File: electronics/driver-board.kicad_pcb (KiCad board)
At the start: 2 copper layers, 40 x 40 mm, 62 parts, among them J1 Conn_01x02, J3 Motor_Conn_01x04, J5 Conn_01x06_Female, SW1 SW_Push, SW2 SW_Push, U2 LMR16020PDDAR, U3 ESP32-C6-MINI-1/U, U4 AMS1117-3.3, U5 TMC5240-TSSOP38, U7 AS5047D

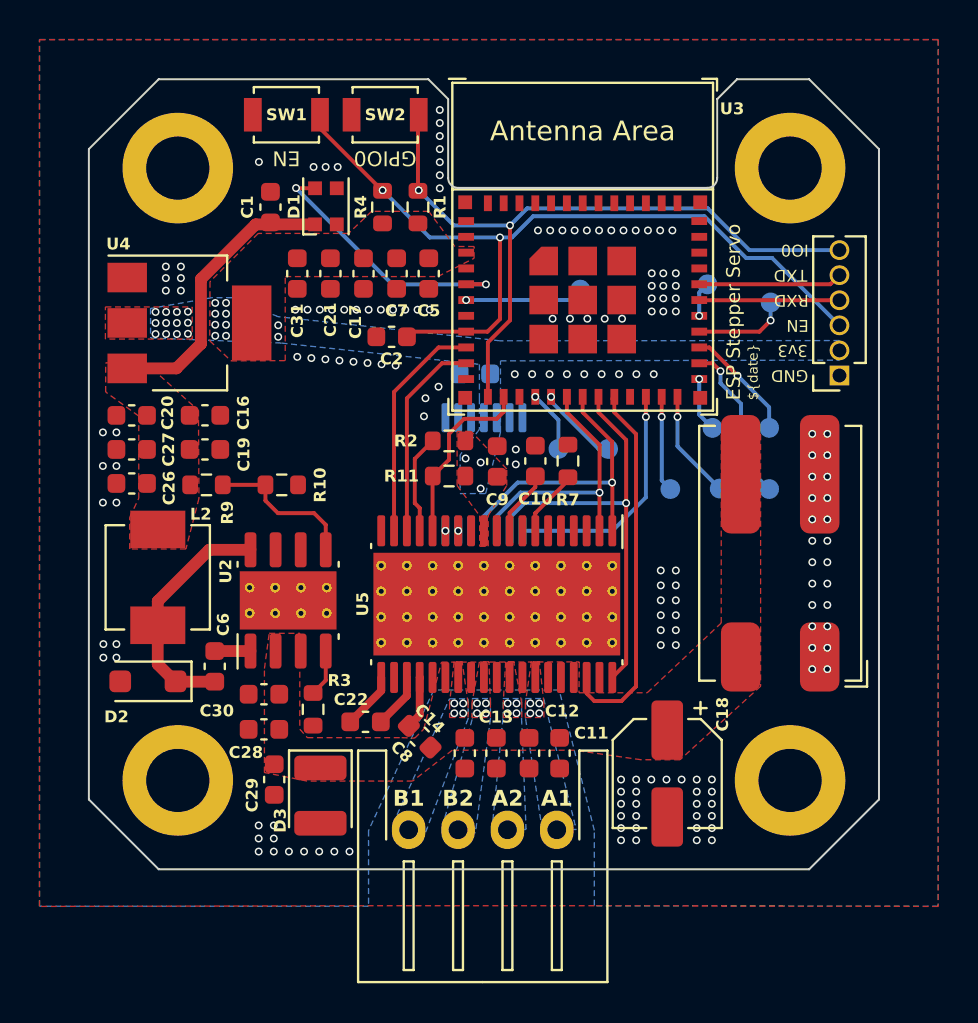
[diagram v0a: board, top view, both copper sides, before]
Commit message: splitted power cap into two and changed connector to wago
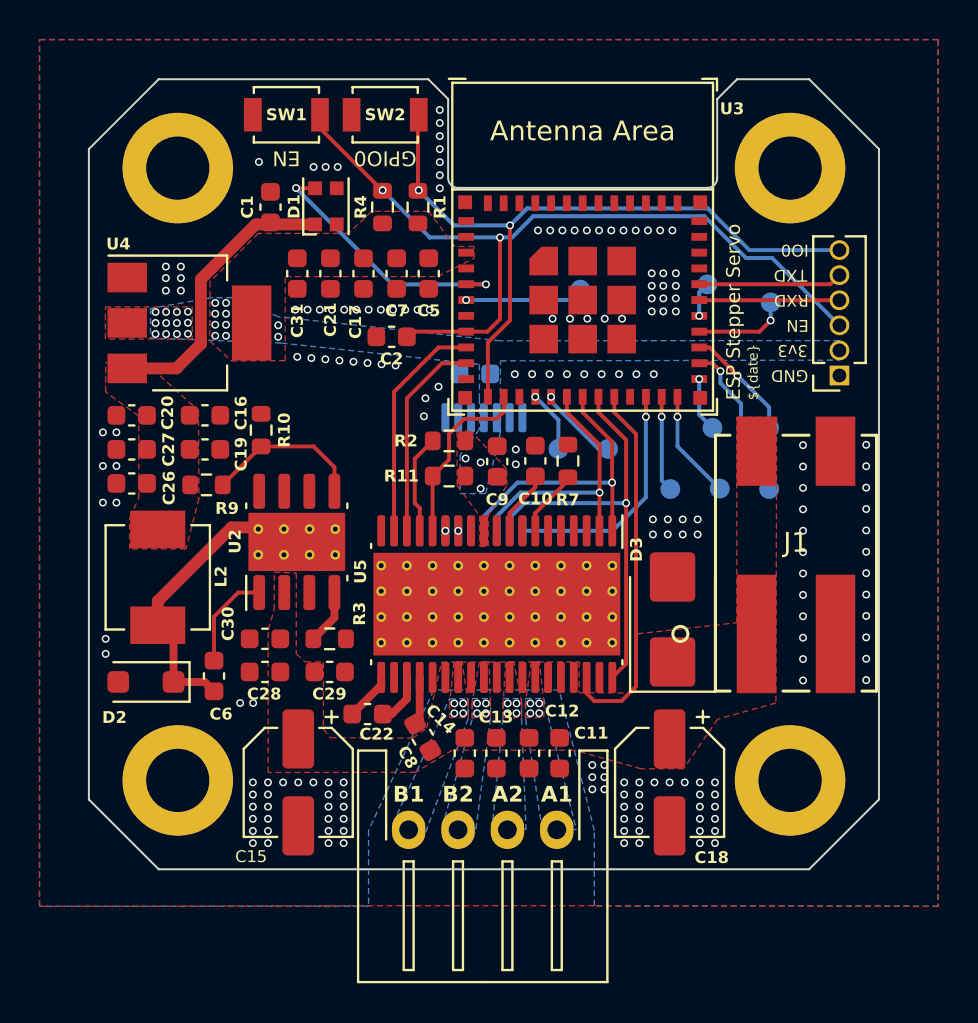
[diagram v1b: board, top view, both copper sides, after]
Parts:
- added C15: 27µF, Capacitor_SMD:CP_Elec_5x5.9, F.Cu at (40.6, 65.6)
- C18: value 47µF -> 27µF
- D3: footprint Diode_SMD:D_1210_3225Metric -> Diode_SMD:D_SMB
- J1: footprint Connector_TE-Connectivity:TE_2834006-2_1x02_P4.0mm_Horizontal -> Slimc_Connector_Wago:2060-472&slash_998-404
- moved D3 19.9 mm to (59.6, 57.3), turned to 90 degrees
- moved C29 6.13 mm to (42.2, 60.0), turned to 180 degrees
- moved R3 3.67 mm to (42.2, 58.3), turned to 180 degrees
- moved U2 2.99 mm to (40.5, 53.4)
- moved R10 2.96 mm to (38.7, 47.8), turned to -90 degrees
- moved C28 2.91 mm to (38.9, 60.0)
- moved C30 2.81 mm to (38.9, 58.3)
- moved J1 0.94 mm to (65.8, 54.5), turned to 0 degrees
- moved C6 0.49 mm to (36.3, 60.2)
- moved C18 0.46 mm to (59.4, 65.6)
- moved C22 0.41 mm to (44.1, 62.1)
- moved C8 0.15 mm to (46.9, 63.3), turned to -60 degrees
- moved D2 0.10 mm to (32.9, 60.5)
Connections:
- J1 pad 1: GND -> VBUS
- J1 pad 2: VBUS -> GND
- U5 pad 39: (no net) -> GND
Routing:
- net Net-(U2-BOOT): track 1.81 -> 5.02 mm
- net Net-(U2-FB): track 7.78 -> 9.38 mm
- net Net-(D2-K): track 12.2 -> 13.1 mm
- net GND: vias 164 -> 182

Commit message: fixed tmc5240 fp and esp32 boot pins
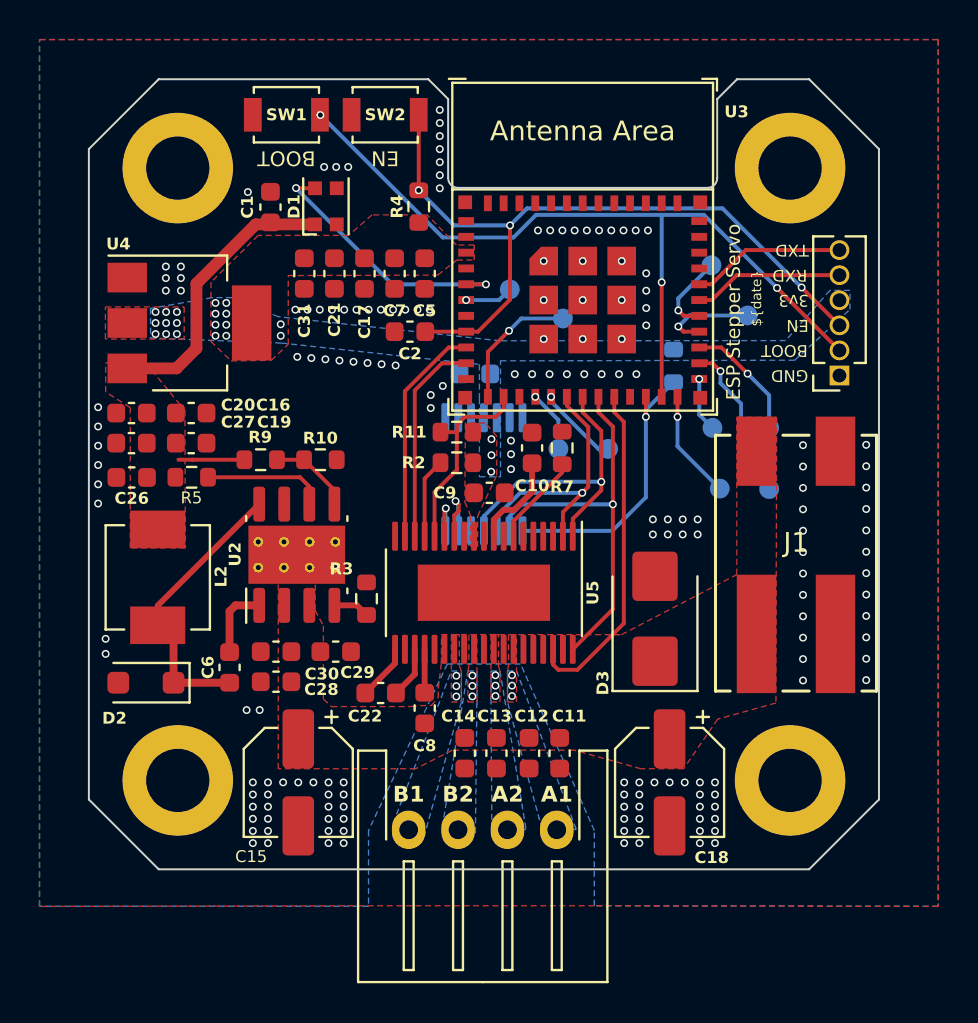
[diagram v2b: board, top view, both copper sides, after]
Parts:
- added R5: 100K, Resistor_SMD:R_0603_1608Metric, F.Cu at (35.2, 50.2)
- R1: moved to B.Cu
- U5: footprint Package_SO:HTSSOP-38-1EP_6.1x12.5mm_P0.65mm_EP5.2x12.5mm_Mask3.39x6.35mm_ThermalVias -> Slimc_Package_SO:TSSOP-38_4.4x9.7mm_P0.5mm
- moved R1 15.2 mm to (59.6, 44.5), turned to -90 degrees
- moved TP9 10.2 mm to (54.0, 42.1)
- moved TP6 3.57 mm to (51.3, 40.6)
- moved R10 3.35 mm to (41.7, 49.3), turned to 180 degrees
- moved R9 3.02 mm to (38.7, 49.3)
- moved R3 2.76 mm to (44.1, 56.3), turned to -90 degrees
- moved R11 2.26 mm to (48.6, 47.9)
- moved R4 1.83 mm to (46.7, 36.4)
- moved C9 1.64 mm to (50.3, 50.9), turned to 180 degrees
- moved C8 1.48 mm to (47.0, 61.8), turned to -90 degrees
- moved TP4 1.34 mm to (63.3, 42.0)
- moved C22 1.26 mm to (44.8, 61.1)
- moved R2 1.17 mm to (48.6, 49.4)
- moved C29 1.07 mm to (42.5, 59.0)
- moved TP5 0.99 mm to (61.5, 39.4)
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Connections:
- J5 pad 2: +3V3 -> /ESP_BOOT
- J5 pad 4: /ESP_UART_RXD -> +3V3
- J5 pad 5: /ESP_UART_TXD -> /ESP_UART_RXD
- J5 pad 6: /ESP_IO0 -> /ESP_UART_TXD
- R1 pad 2: /ESP_IO0 -> /SPI_CSN_ENC
- SW1 pad 2: /ESP_EN -> /ESP_BOOT
- SW2 pad 2: /ESP_IO0 -> /ESP_EN
- TP9 pad 1: Net-(U3-GPIO9) -> Net-(U3-GPIO0/ADC1_CH0/XTAL_32K_P)
- U2 pad 3: unconnected-(U2-EN-Pad3) -> VBUS
- U2 pad 6: unconnected-(U2-PGOOD-Pad6) -> Net-(U2-PGOOD)
- U3 pad 12: /ESP_IO0 -> Net-(U3-GPIO0/ADC1_CH0/XTAL_32K_P)
- U3 pad 23: Net-(U3-GPIO9) -> /ESP_BOOT
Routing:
- net /ESP_BOOT: track 0.00 -> 42.1 mm, vias 0 -> 3
- net /ESP_IO0: track 36.3 -> 0.00 mm, vias 2 -> 0
- net Net-(U3-GPIO0/ADC1_CH0/XTAL_32K_P): track 0.00 -> 6.78 mm, vias 0 -> 1
- net Net-(U2-PGOOD): track 0.00 -> 6.39 mm
- net Net-(U2-FB): track 9.38 -> 4.26 mm
- net Net-(U3-GPIO9): track 4.85 -> 0.00 mm, vias 1 -> 0
- net /ESP_EN: track 41.3 -> 37.5 mm, vias 2 -> 3
- net Net-(U3-GPIO3/ADC1_CH3): track 6.00 -> 2.46 mm
- net Net-(U5-ENCB): track 0.00 -> 3.49 mm
- net +5V: track 14.4 -> 17.8 mm
- net Net-(U5-ENCA): track 0.00 -> 2.58 mm
- net Net-(U3-GPIO23): track 1.77 -> 4.15 mm
- net /SPI_CSN_ENC: track 12.0 -> 14.4 mm
- net /SPI_SCK: track 22.0 -> 20.2 mm
- net /SPI_CSN_TMC: track 19.0 -> 17.2 mm
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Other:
- board text added: "BOOT"
- board text removed: "GPIO0"
- board text removed: "IO9"

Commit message: power labels
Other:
- board text added: "+"
- board text added: "-"
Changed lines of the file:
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@@
     (effects (font (size 0.6 0.6) (thickness 0.1)) (justify left))
+  )
+  (gr_text "+" (at 63.799999 61.8744) (layer "F.SilkS")
+    (effects (font (size 1.5 1.5) (thickness 0.3) bold))
   )
   (gr_text "A2" (at 51.19 66.2052) (layer "F.SilkS" knockout)
@@
     (effects (font (size 0.6 0.6) (thickness 0.1)) (justify left))
   )
+  (gr_text "-" (at 67.800001 61.8744) (layer "F.SilkS")
+    (effects (font (size 1.5 1.5) (thickness 0.3) bold))
+  )
   (gr_text "B1" (at 46.19 66.2052) (layer "F.SilkS" knockout)

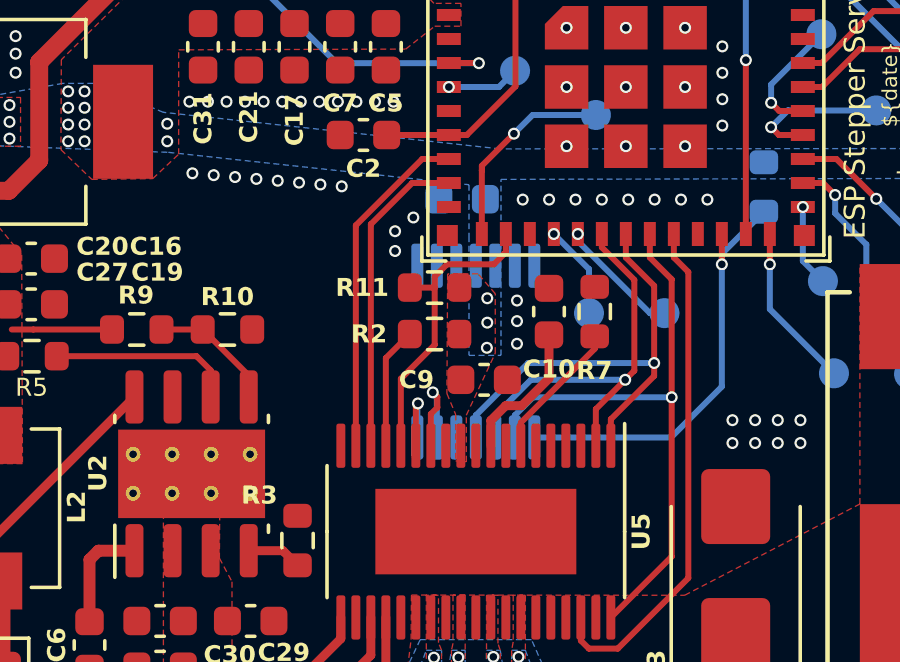
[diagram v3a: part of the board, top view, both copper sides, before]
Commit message: connected encoder index
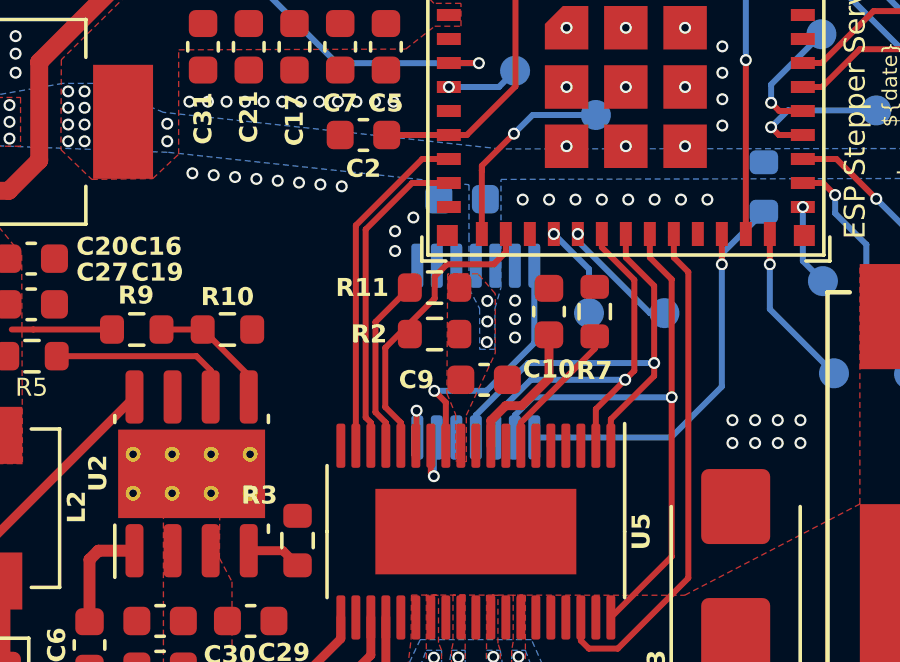
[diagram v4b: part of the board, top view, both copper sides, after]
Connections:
- R11 pad 2: /TMC_ENABLE -> Net-(U5-UART_EN)
- R2 pad 2: Net-(U5-UART_EN) -> /TMC_ENABLE
- U5 pad 12: /TMC_ENCN -> Net-(U5-ENCN)
- U7 pad 14: unconnected-(U7-I/PWM-Pad14) -> Net-(U5-ENCN)
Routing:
- net Net-(U5-ENCN): track 0.00 -> 8.56 mm, vias 0 -> 1
- net Net-(U5-UART_EN): track 4.05 -> 5.98 mm
- net Net-(U5-ENCB): track 3.49 -> 2.39 mm

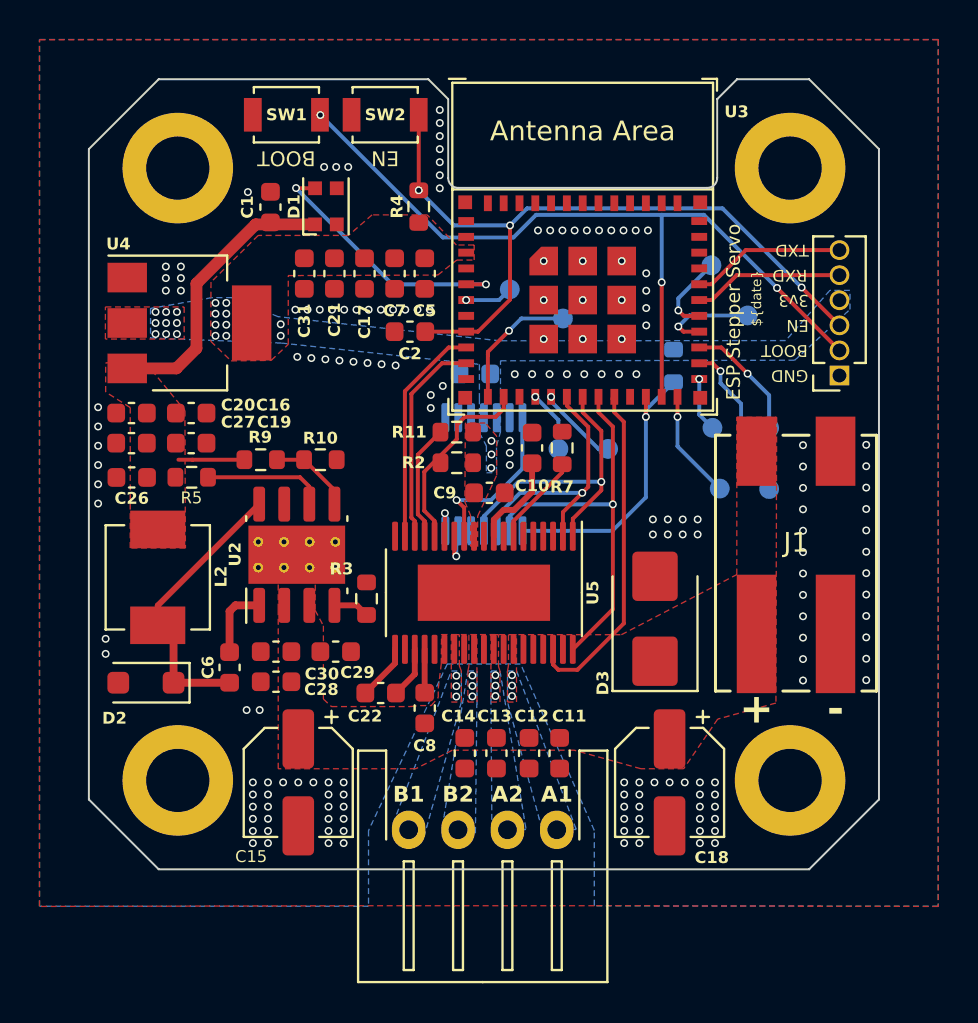
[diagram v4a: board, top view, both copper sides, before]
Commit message: new board layout; stripped 5v line and added qwiic and some buttons
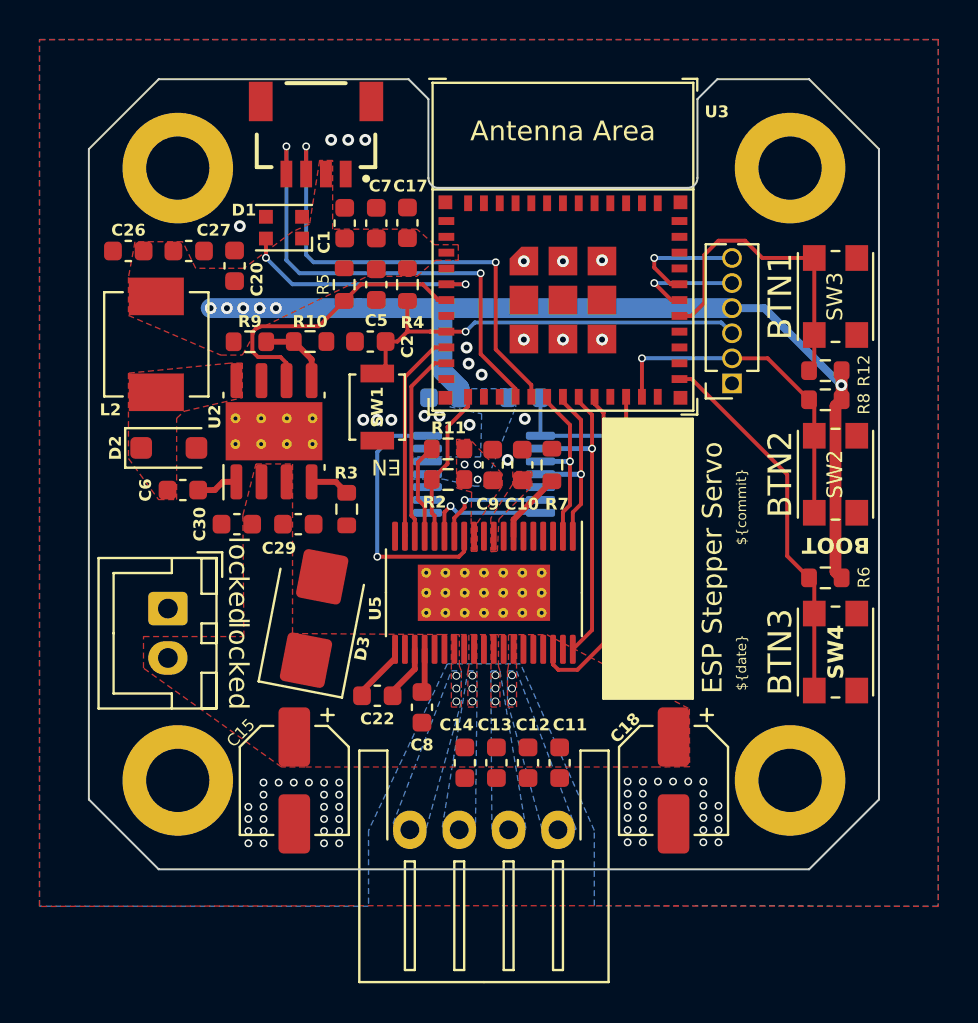
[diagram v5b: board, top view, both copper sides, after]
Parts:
- removed C16, C21: 4.7µF, Capacitor_SMD:C_0603_1608Metric
- removed C19, C31: 1µF, Capacitor_SMD:C_0603_1608Metric
- removed C28: 2.2µF, Capacitor_SMD:C_0603_1608Metric
- removed TP1, TP10, TP2, TP3, TP4, TP5, TP6, TP7, TP8, TP9: TestPoint, TestPoint:TestPoint_Pad_D1.0mm
- removed U4: AMS1117-3.3, Package_TO_SOT_SMD:SOT-223-3_TabPin2
- added J4: Qwiic_RA, SparkFun-Connector:JST04_1MM_RA, F.Cu at (41.5, 34.8)
- added R12: 10k, Resistor_SMD:R_0603_1608Metric, F.Cu at (67.3, 44.8)
- added R6: 10k, Resistor_SMD:R_0603_1608Metric, F.Cu at (67.3, 55.2)
- added R8: 10k, Resistor_SMD:R_0603_1608Metric, F.Cu at (67.3, 46.2)
- added SW2: SW_Push, Slimc_Button_Switch_SMD:SW_Push_1P1T_TS-1145-X-B, F.Cu at (67.8, 50.0)
- added SW4: SW_Push, Slimc_Button_Switch_SMD:SW_Push_1P1T_TS-1145-X-B, F.Cu at (67.8, 59.0)
- C15, C18: value 27µF -> 33µF
- J1: footprint Slimc_Connector_Wago:2060-472&slash_998-404 -> Connector_JST:JST_XH_B2B-XH-A_1x02_P2.50mm_Vertical
- J3: value Motor_Conn_01x04 -> S4B-XH-A
- R1, R11, R2, R4: value 10K -> 10k
- R10: value 17.4K -> 28.7k
- R3: value 41.2K -> 41.2k
- R5, R9: value 100K -> 100k
- R7: value 12K -> 12k
- SW3: renamed from SW1; footprint Button_Switch_SMD:SW_SPST_B3U-1000P -> Slimc_Button_Switch_SMD:SW_Push_1P1T_TS-1145-X-B
- moved J1 31.9 mm to (34.0, 56.8), turned to -90 degrees
- moved SW3 29.3 mm to (67.8, 41.0), turned to -90 degrees
- moved D3 17.3 mm to (41.4, 57.3), turned to 79 degrees
- moved SW1 14.8 mm to (44.6, 46.6), turned to -90 degrees
- moved R5 12.4 mm to (42.9, 40.4), turned to -90 degrees
- moved D2 11.9 mm to (34.0, 48.7), turned to 0 degrees
- moved L2 11.8 mm to (33.4, 43.4)
- moved C26 11.5 mm to (32.0, 38.7)
- moved C27 10.2 mm to (35.1, 38.7), turned to 180 degrees
- moved C6 9.29 mm to (34.8, 50.8), turned to 0 degrees
- moved C20 9.10 mm to (37.4, 39.4), turned to -90 degrees
- moved R1 7.73 mm to (52.0, 46.1), turned to 180 degrees
- moved C30 6.75 mm to (37.5, 52.5)
- moved C29 6.72 mm to (40.6, 52.5)
- moved U2 6.36 mm to (39.4, 47.8)
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- renumbered SW2 to SW1
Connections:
- C1 pad 1: +5V -> +3V3
- C2 pad 1: GND -> /ESP_EN
- C2 pad 2: /ESP_EN -> GND
- C20 pad 2: +5V -> +3V3
- C26 pad 2: +5V -> +3V3
- C27 pad 2: +5V -> +3V3
- D1 pad 1: +5V -> +3V3
- J1 pad 1: VBUS -> GND
- J1 pad 2: GND -> VBUS
- L2 pad 2: +5V -> +3V3
- R1 pad 1: +3V3 -> /SPI_CSN_ENC
- R1 pad 2: /SPI_CSN_ENC -> +3V3
- R5 pad 1: +5V -> +3V3
- R5 pad 2: Net-(U2-PGOOD) -> /PSU_PGOOD
- R9 pad 2: +5V -> +3V3
- SW1 pad 1: GND -> /ESP_EN
- SW1 pad 2: /ESP_EN -> GND
- SW3 pad 2: /ESP_BOOT -> /SW_BTN1
- U2 pad 6: Net-(U2-PGOOD) -> /PSU_PGOOD
- U3 pad 12: Net-(U3-GPIO0/ADC1_CH0/XTAL_32K_P) -> /TMC_ENABLE
- U3 pad 13: /TMC_ENABLE -> unconnected-(U3-GPIO1/ADC1_CH1/XTAL_32K_N-Pad13)
- U3 pad 15: Net-(U3-MTCK/GPIO6/ADC1_CH6) -> /I2C_SCL
- U3 pad 16: Net-(U3-MTDO/GPIO7) -> /I2C_SDA
- U3 pad 24: Net-(U3-GPIO18) -> unconnected-(U3-GPIO18-Pad24)
- U3 pad 25: Net-(U3-GPIO19) -> /SW_BTN3
- U3 pad 26: Net-(U3-GPIO20) -> unconnected-(U3-GPIO20-Pad26)
- U3 pad 27: Net-(U3-GPIO21) -> unconnected-(U3-GPIO21-Pad27)
- U3 pad 28: Net-(U3-GPIO22) -> unconnected-(U3-GPIO22-Pad28)
- U3 pad 29: Net-(U3-GPIO23) -> /SW_BTN1
- U3 pad 6: Net-(U3-GPIO3/ADC1_CH3) -> /PSU_PGOOD
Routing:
- net +3V3: track 0.00 -> 49.2 mm, vias 22 -> 9
- net /ESP_BOOT: track 42.1 -> 17.1 mm, vias 3 -> 1
- net /I2C_SCL: track 0.00 -> 24.3 mm, vias 0 -> 2
- net /I2C_SDA: track 0.00 -> 24.2 mm, vias 0 -> 2
- net /SW_BTN3: track 0.00 -> 19.0 mm
- net +5V: track 17.8 -> 0.00 mm
- net /SW_BTN1: track 0.00 -> 16.0 mm
- net /ESP_EN: track 37.5 -> 21.5 mm, vias 3 -> 1
- net /PSU_PGOOD: track 0.00 -> 15.5 mm
- net Net-(D2-K): track 14.3 -> 0.00 mm
- net Net-(U3-GPIO20): track 8.23 -> 0.00 mm, vias 1 -> 0
- net Net-(U3-GPIO0/ADC1_CH0/XTAL_32K_P): track 6.78 -> 0.00 mm, vias 1 -> 0
- net Net-(U2-PGOOD): track 6.39 -> 0.00 mm
- net Net-(U3-GPIO21): track 6.19 -> 0.00 mm, vias 1 -> 0
- net /SPI_CSN_ENC: track 14.4 -> 8.23 mm
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- added copper zone on F.Cu, net Net-(D2-K)
- added copper zone on F.Cu, net Net-(U5-VDD1V8)
- removed copper zone on F.Cu, net +5V
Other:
- outline, holes or cut-outs redrawn
- board text added: "${commit}"
- board text added: "BTN1"
- board text added: "BTN2"
- board text added: "BTN3"
- board text added: "GND BOOT EN 3v3 RXD TXD"
- board text added: "locked"
- board text removed: "+"
- board text removed: "-"
- board text removed: "3v3"
- board text removed: "GND"
- board text removed: "IO0"
- board text removed: "IO18"
- board text removed: "IO19"
- board text removed: "IO20"
- board text removed: "IO21"
- board text removed: "IO22"
- board text removed: "IO23"
- board text removed: "IO3"
- board text removed: "IO6"
- board text removed: "IO7"
- board text removed: "RXD"
- board text removed: "TXD"
